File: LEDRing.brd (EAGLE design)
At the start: 100 x 80 mm, 11 parts, among them U1 ATMEGA328P-AU, Y1 16MHZ

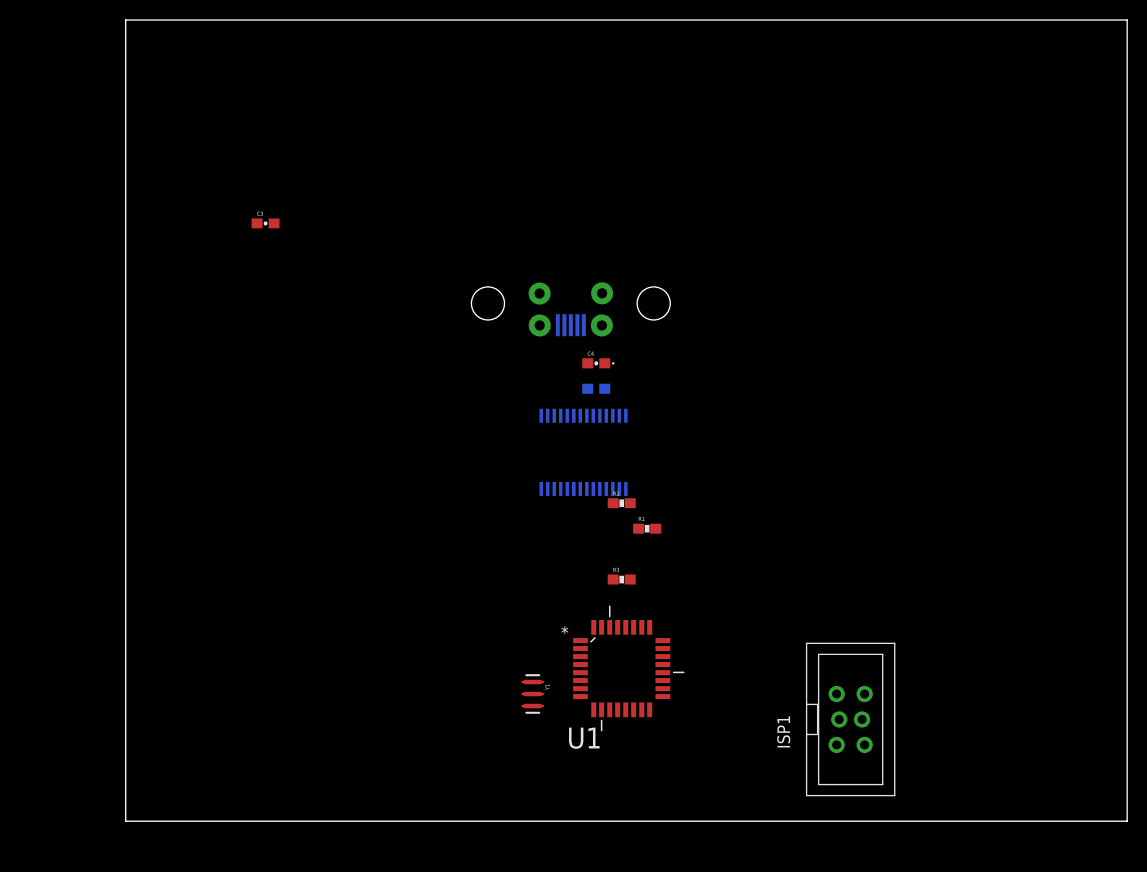
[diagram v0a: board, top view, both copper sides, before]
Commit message: Added accelerometer Added power Added LEDs
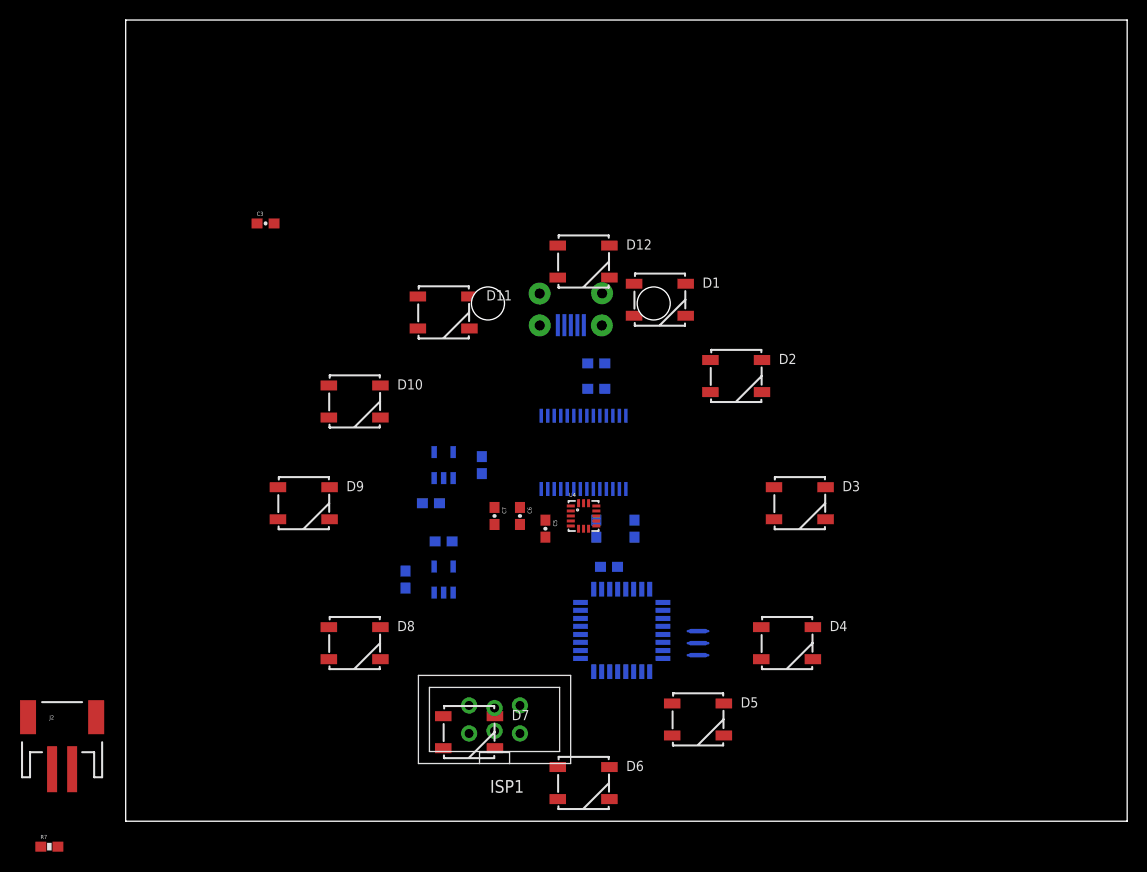
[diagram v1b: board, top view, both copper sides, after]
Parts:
- added C1: 47uF, SparkFun-Capacitors:0603-CAP
- added C5, C7: 0.1uF, SparkFun-Capacitors:0603-CAP
- added C6: 4.7uF, SparkFun-Capacitors:0603-CAP
- added D1, D10, D11, D12, D2, D3, D4, D5, D6, D7, D8, D9: (no value), SparkFun-LED:WS2812B
- added J2: (no value), SparkFun-Connectors:JST-2-SMD
- added R4, R7: (no value), SparkFun-Passives:0603-RES
- added R5, R6: 10k, SparkFun-Passives:0603-RES
- added U2: MCP73831, SparkFun-PowerIC:SOT23-5
- added U3: MIC5219 3.3V, SparkFun-PowerIC:SOT23-5
- added U4: MMA8452Q, SparkFun-Sensors:QFN-16_0.5MM
- R3: value (none) -> 10k
- moved ISP1 35.6 mm to (36.8, 10.2), turned to 90 degrees
- moved Y1 17.3 mm to (57.1, 17.8), flipped to the bottom, turned to 90 degrees
- moved U1 3.81 mm to (49.5, 19.1), flipped to the bottom
- moved R2 3.59 mm to (47.0, 29.2), flipped to the bottom, turned to 90 degrees
- moved R3 1.80 mm to (48.3, 25.4), flipped to the bottom, turned to 180 degrees
- moved R1 1.27 mm to (50.8, 29.2), flipped to the bottom, turned to 90 degrees
- flipped C4 to the bottom
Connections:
- removed net AVCC: U1.18
- removed net N$12: ISP1.2
- removed net VCC: U1.6
- removed net VCC_2: U1.4
- new net 5V: C1.1, C2.1, C4.A, J1.1, U$1.20, U2.4
- new net LED_DATA: R7.2
- new net N$10: R7.1, U1.10
- new net N$9: R4.2, U2.5
- new net SCL: R5.1, U1.28, U4.4
- new net SDA: R6.1, U1.27, U4.6
- new net V3_3: C3.1, C6.1, C7.1, ISP1.2, R3.2, R5.2, R6.2, U1.18, U1.4, U1.6, U3.5, U4.1, U4.14
- new net VBATT: J2.2, U2.3, U3.1, U3.3
- new net VDD: D1.1, D10.1, D11.1, D12.1, D2.1, D3.1, D4.1, D5.1, D6.1, D7.1, D8.1, D9.1
- new net VSS: D1.3, D10.3, D11.3, D12.3, D2.3, D3.3, D4.3, D5.3, D6.3, D7.3, D8.3, D9.3
- net GND: now also C1.2, C3.2, C5.2, C6.2, C7.2, J2.1, R4.1, U2.2, U3.2, U4.10, U4.12, U4.5, U4.7
- net N$3: now also C5.1, U4.2; no longer C2.1, C4.A, J1.1, U$1.20
- net RX: now also U4.9
- net TX: now also U4.11

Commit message: More updates to layout
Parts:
- removed J2: (no value), SparkFun-Connectors:JST-2-SMD
- added J3: (no value), SparkFun-Connectors:1X02
- moved D3 63.7 mm to (3.81, 26.5), turned to 90 degrees
- moved D4 62.3 mm to (6.48, 36.1), turned to 60 degrees
- moved D2 61.1 mm to (7.24, 15.4), turned to 300 degrees
- moved D1 59.3 mm to (15.1, 6.73), turned to 150 degrees
- moved D12 55.4 mm to (26.4, 3.94), turned to 180 degrees
- moved R7 55.1 mm to (20.3, 45.0), flipped to the bottom, turned to 90 degrees
- moved D5 55.0 mm to (14.4, 44.7), turned to 210 degrees
- moved D6 48.5 mm to (26.0, 48.1), turned to 180 degrees
- moved Y1 47.8 mm to (14.7, 39.9)
- moved D11 44.2 mm to (36.6, 6.86), turned to 30 degrees
- moved D7 36.4 mm to (37.1, 45.2), turned to 150 degrees
- moved D10 34.9 mm to (45.0, 14.9), turned to 240 degrees
- moved C4 34.7 mm to (30.9, 15.0), turned to 225 degrees
- moved R3 33.3 mm to (15.7, 32.6), turned to 45 degrees
- moved U1 32.8 mm to (22.4, 37.5), turned to 180 degrees
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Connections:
- new net LED_CONT: D6.2, D7.3
- new net N$14: D1.1
- new net N$15: D1.2, D2.4
- new net N$16: D2.2, D3.4
- new net N$17: D3.2, D4.4
- new net N$18: D4.2, D5.4
- new net N$19: D5.2, D6.4
- new net N$20: D7.2, D8.4
- new net N$21: D8.2, D9.4
- new net N$22: D10.4, D9.2
- new net N$23: D10.2, D11.4
- new net N$24: D11.2, D12.4
- net GND: now also J3.2; no longer J2.1
- net VBATT: now also J3.1; no longer J2.2
- net VDD: no longer D1.1
- net VSS: no longer D7.3
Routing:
- net V3_3: track 0.00 -> 61.0 mm, vias 0 -> 3
- net GND: track 0.00 -> 39.3 mm, vias 0 -> 2
- net RESET: track 0.00 -> 33.8 mm
- net VBATT: track 0.00 -> 17.9 mm, vias 0 -> 2
- net MISO: track 0.00 -> 17.4 mm
- net SCL: track 0.00 -> 15.7 mm
- net MOSI: track 0.00 -> 13.9 mm, vias 0 -> 1
- net SCK: track 0.00 -> 12.6 mm
- net RX: track 0.00 -> 9.59 mm, vias 0 -> 2
- net TX: track 0.00 -> 9.58 mm, vias 0 -> 1
- net SDA: track 0.00 -> 8.58 mm, vias 0 -> 2
- net N$2: track 0.00 -> 5.20 mm
- net N$1: track 0.00 -> 4.61 mm
- net N$7: track 0.00 -> 2.89 mm
- net N$8: track 0.00 -> 2.82 mm
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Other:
- board size 100 x 80 mm -> 52.5 x 52.4 mm

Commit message: Updated schematics
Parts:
- moved J1 3.56 mm to (43.2, 26.5)
- moved D4 1.05 mm to (7.04, 37.0)
- moved D5 0.83 mm to (15.1, 45.0), turned to 30 degrees
- moved D3 0.68 mm to (4.06, 25.9)
- moved D11 0.64 mm to (37.2, 6.78), turned to 210 degrees
- moved D2 0.55 mm to (7.04, 14.9), turned to 120 degrees
- moved D8 0.42 mm to (45.3, 37.0), turned to 300 degrees
- moved D10 0.33 mm to (45.3, 14.9)
- moved D12 0.28 mm to (26.2, 3.81)
- moved D7 0.22 mm to (37.2, 45.0), turned to 330 degrees
- moved D6 0.18 mm to (26.2, 48.0), turned to 0 degrees
- moved D1 0.05 mm to (15.1, 6.78)
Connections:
- removed net N$14: D1.1
- net VBATT: now also D1.1, D2.1, D3.1, D4.1, D5.1, D6.1
- net VDD: no longer D2.1, D3.1, D4.1, D5.1, D6.1
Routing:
- net N$17: track 0.00 -> 18.5 mm
- net N$18: track 0.00 -> 18.4 mm
- net N$16: track 0.00 -> 18.1 mm
- net N$15: track 0.00 -> 18.0 mm
- net GND: track 39.3 -> 42.9 mm
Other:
- outline, holes or cut-outs redrawn

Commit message: More routing done
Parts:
- added BAT1: (no value), SparkFun-Electromechanical:BATTCON_12MM
- added U$2: DS3234, SparkFun-FreqCtrl:DS3234
- added U5: HMC5883LSMD, SparkFun-Sensors:16LPCC
- moved J3 18.6 mm to (21.7, 11.4), turned to 0 degrees
- moved J1 13.7 mm to (56.9, 27.2)
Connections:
- removed net VDD: D10.1, D11.1, D12.1, D7.1, D8.1, D9.1
- new net +: BAT1.PWR@1
- new net -: BAT1.GND
- net LED_CONT: now also D7.4; no longer D7.3
- net VBATT: now also D10.1, D11.1, D12.1, D7.1, D8.1, D9.1
- net VSS: now also D7.3
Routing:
- net VBATT: track 17.9 -> 172.3 mm, vias 2 -> 4
- net VSS: track 0.00 -> 124.2 mm
- net N$21: track 0.00 -> 28.5 mm, vias 0 -> 4
- net N$22: track 0.00 -> 25.5 mm, vias 0 -> 2
- net N$24: track 0.00 -> 25.1 mm, vias 0 -> 2
- net N$19: track 0.00 -> 24.3 mm, vias 0 -> 2
- net N$20: track 0.00 -> 24.1 mm, vias 0 -> 2
- net LED_CONT: track 0.00 -> 24.0 mm, vias 0 -> 2
- net N$23: track 0.00 -> 23.8 mm, vias 0 -> 2
- net N$18: track 18.4 -> 24.7 mm, vias 0 -> 2
- net N$17: track 18.5 -> 24.6 mm, vias 0 -> 2
- net GND: track 42.9 -> 37.0 mm
- net N$15: track 18.0 -> 23.1 mm, vias 0 -> 2

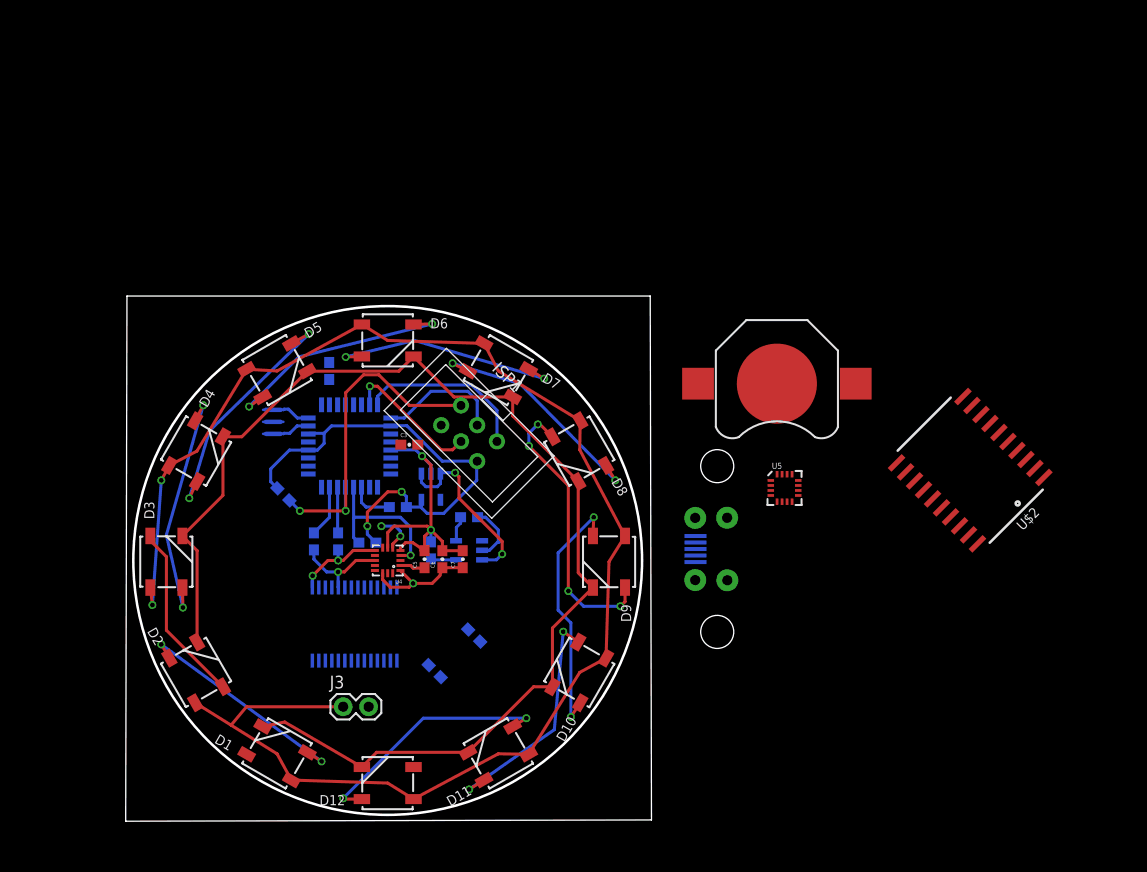
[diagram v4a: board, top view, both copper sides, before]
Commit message: Moved USB connector
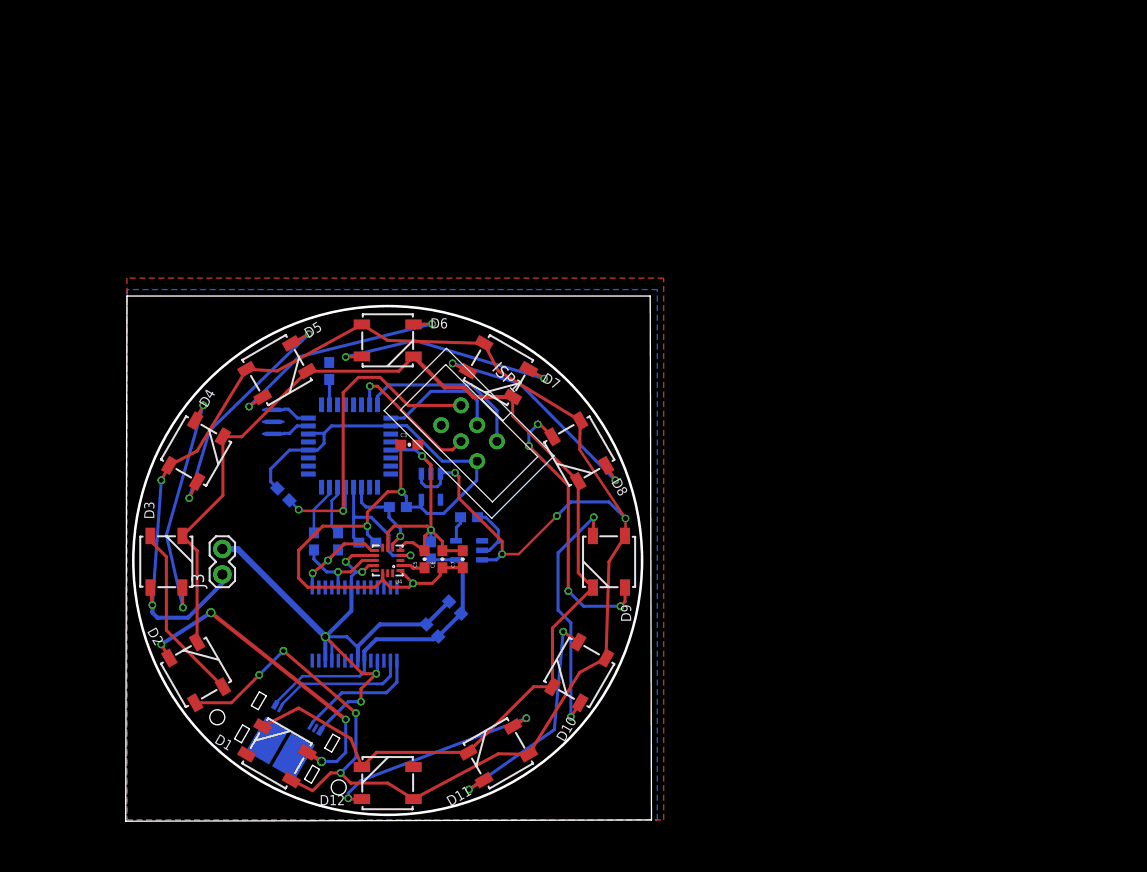
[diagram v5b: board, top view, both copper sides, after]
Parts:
- removed BAT1: (no value), SparkFun-Electromechanical:BATTCON_12MM
- removed J1: (no value), SparkFun-Connectors:MICRO-B-SMT
- removed U5: HMC5883LSMD, SparkFun-Sensors:16LPCC
- U$2: value DS3234 -> TE_USB_A121025CT; device SparkFun-FreqCtrl:DS3234 -> LEDRingLib:TE_USB_A121025CT
- moved U$2 76.1 mm to (14.3, 5.32), flipped to the bottom, turned to 210 degrees
- moved J3 17.9 mm to (9.65, 24.6), turned to 90 degrees
- moved C4 4.07 mm to (30.6, 19.1)
- moved C2 3.38 mm to (32.9, 21.3)
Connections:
- net N$6 renamed VCCIO
- removed net +: BAT1.PWR@1
- removed net -: BAT1.GND
- new net VSTAT: U2.1
- net 5V: now also U$2.P$1; no longer J1.1
- net GND: now also U$2.P$5; no longer J1.5
- net N$4: now also U$2.P$2; no longer J1.2
- net N$5: now also U$2.P$3; no longer J1.3
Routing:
- net GND: track 37.0 -> 104.6 mm, vias 2 -> 7
- net VBATT: track 172.3 -> 201.9 mm, vias 4 -> 10
- net 5V: track 2.55 -> 32.1 mm
- net V3_3: track 61.0 -> 86.1 mm
- net N$4: track 0.00 -> 13.9 mm
- net N$5: track 0.00 -> 12.6 mm
- net N$15: track 23.1 -> 32.5 mm, vias 2 -> 4
- net N$10: track 0.00 -> 2.54 mm
- net N$24: track 25.1 -> 22.9 mm
- net VSS: track 124.2 -> 126.1 mm
- net RX: track 9.59 -> 10.9 mm
- net SDA: track 8.58 -> 9.36 mm, vias 2 -> 1
- net SCL: track 15.7 -> 15.1 mm, vias 0 -> 1
- net N$1: track 4.61 -> 5.12 mm
- net RESET: track 33.8 -> 33.6 mm, vias 0 -> 2
- added copper zone on layer 1, net GND
- added copper zone on layer 16, net GND
